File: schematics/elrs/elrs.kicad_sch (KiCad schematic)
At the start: 34 parts, among them U13 ESP32-C3FH4, U14 TLV75533PDQNR, U15 SX1281IMLTRT, X2 CJ17-400001010B20

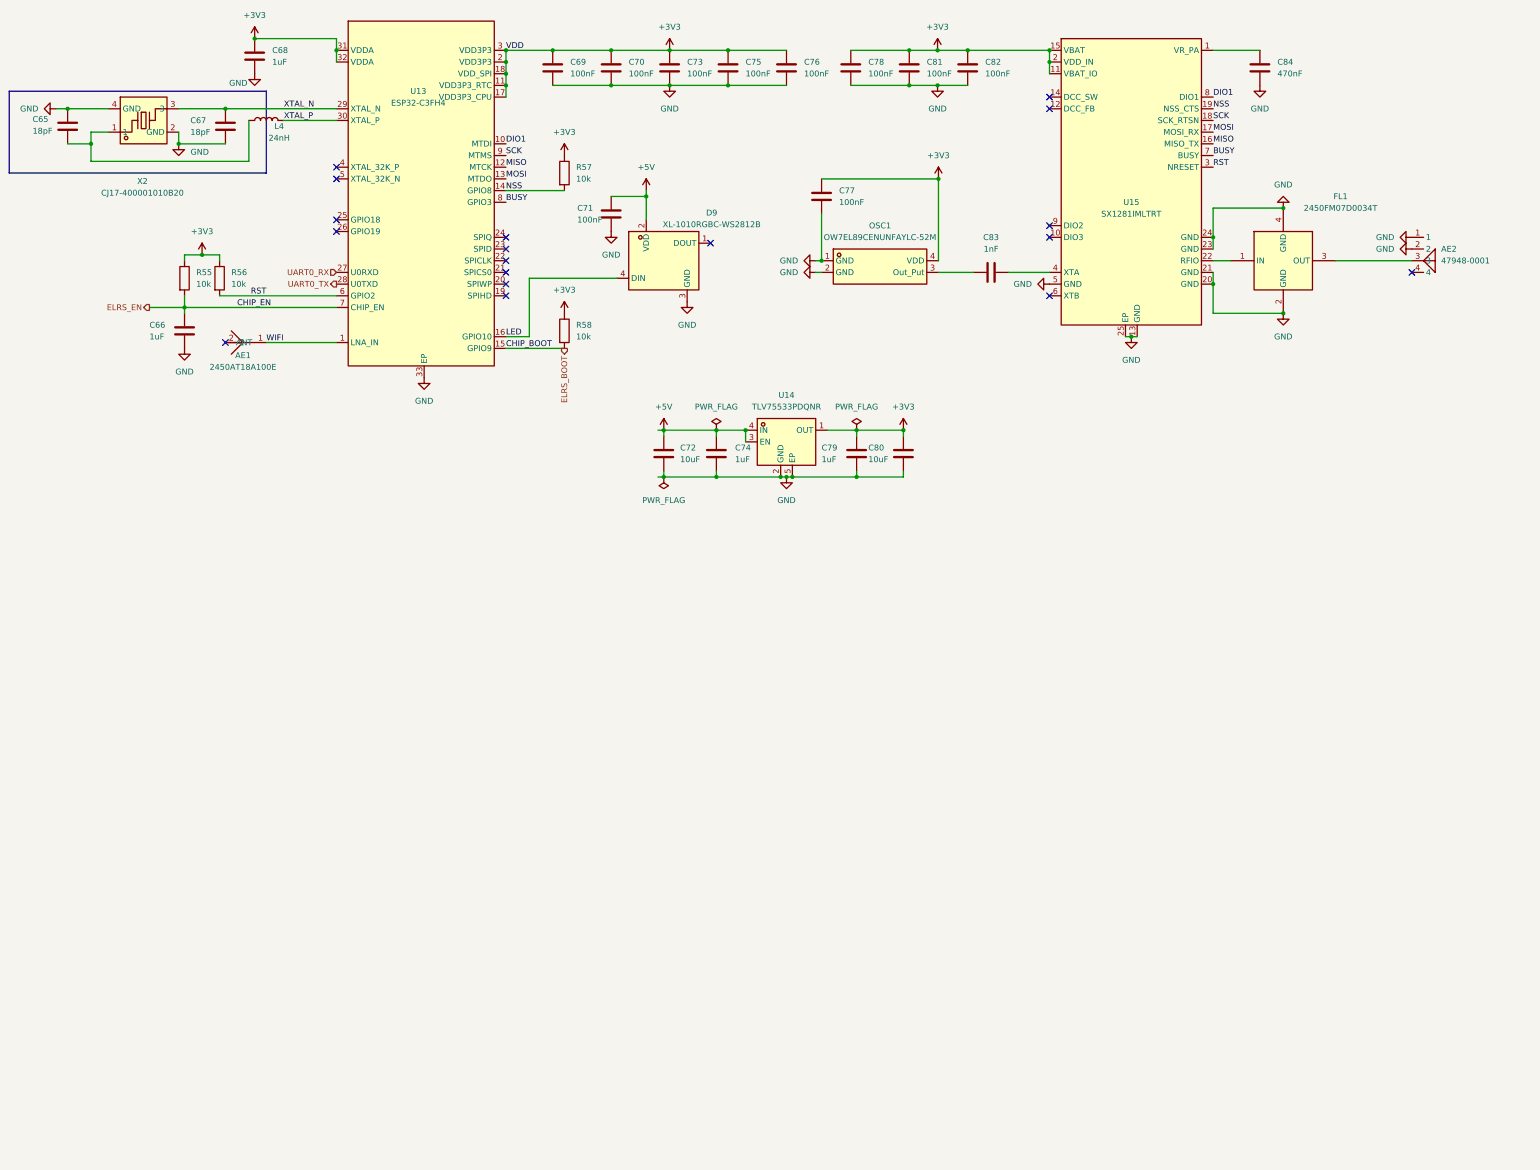
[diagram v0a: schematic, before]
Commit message: checkpoint: Bluejay/BLHeli_S part imports + ESC rework notes
EFM8BB51F16G (C6547511), AGM310MAP (C5184858), BY25Q64ESCIG (C50176394)
imported into libs/lib.kicad_sym + lib.pretty + lib.3dshapes.
BLHELI_S_ESC_NOTES.md documents gate-drive research (1S direct drive vs
2S level-shift requirement) and open design decisions.

Co-Authored-By: Claude Fable 5 <noreply@anthropic.com>
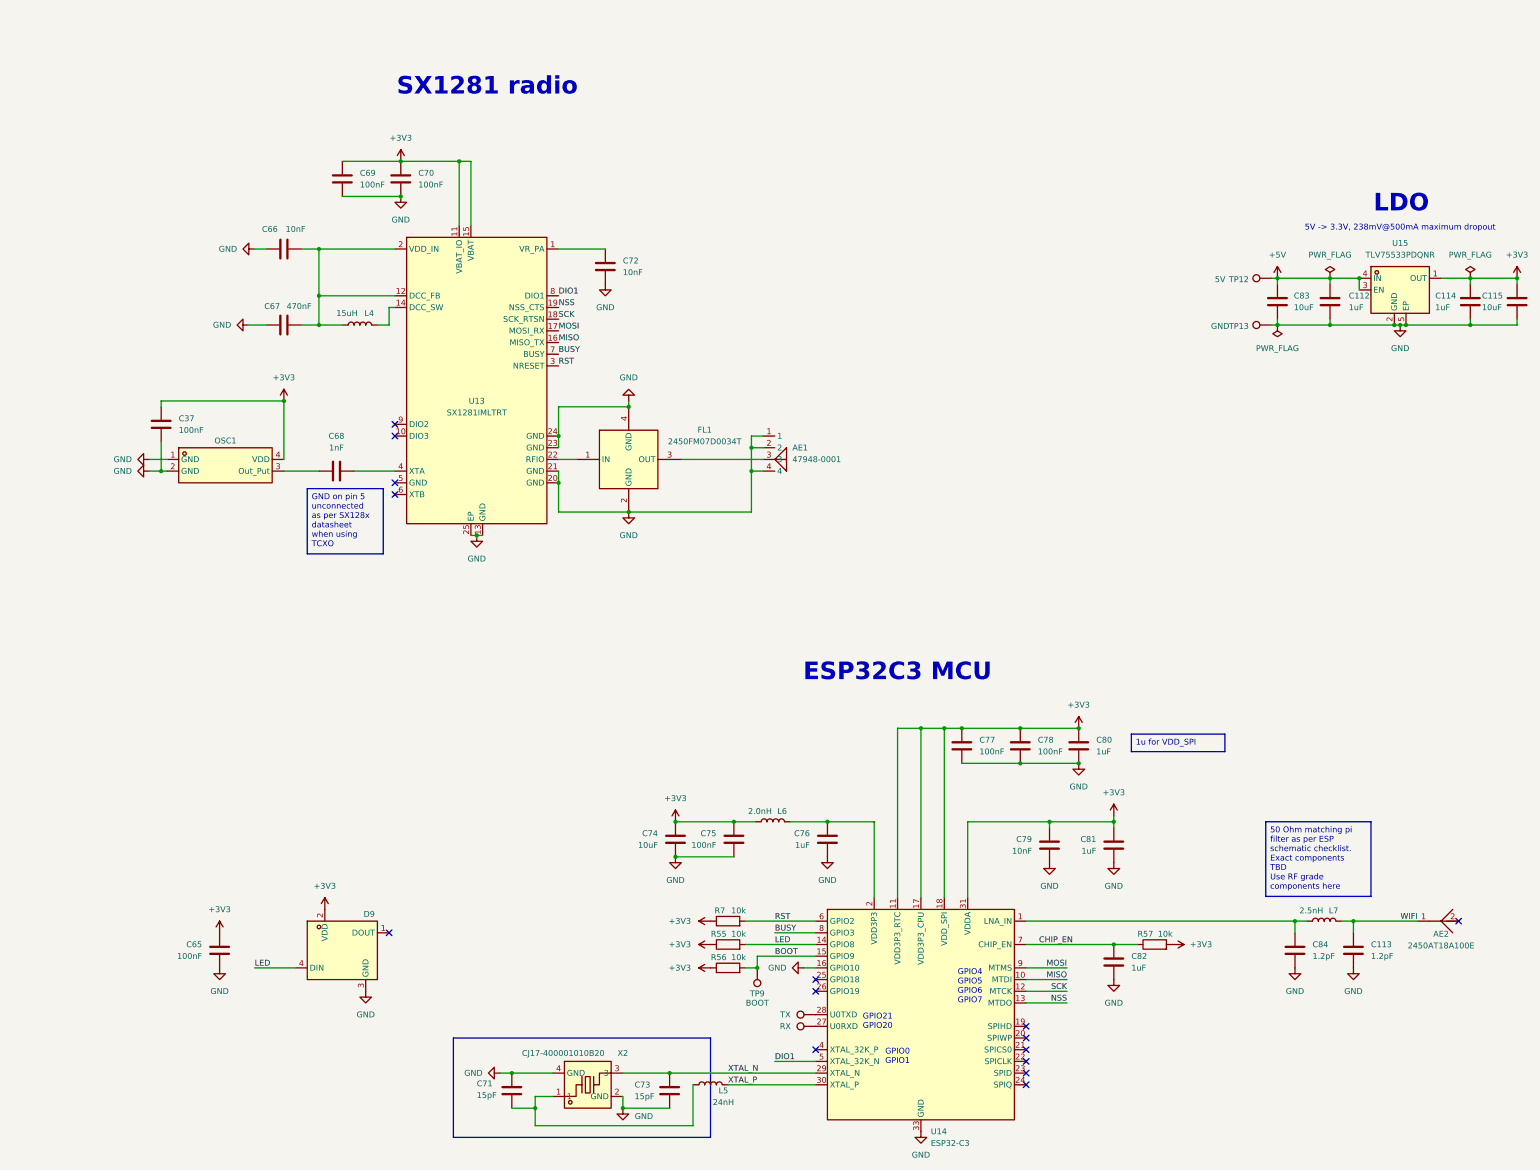
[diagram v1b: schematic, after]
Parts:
- removed AE1: 2450AT18A100E, lib:ANT-SMD_L3.2-W1.6, symbol lib:2450AT18A100E
- removed AE2: 47948-0001, lib:ANT-SMD_47948-0001, symbol lib:47948-0001
- removed C68: 1uF, Capacitor_SMD:C_0201_0603Metric, symbol Device:C
- removed D9: XL-1010RGBC-WS2812B, lib:LED-SMD_4P-L1.0-W1.0-TL_XL-1010RGBC-WS2812B, symbol lib:XL-1010RGBC-WS2812B
- removed FL1: 2450FM07D0034T, lib:FILTER-SMD_4P-L1.0-W0.5-L, symbol lib:2450FM07D0034T
- removed R58: 10k, Resistor_SMD:R_0201_0603Metric, symbol Device:R
- removed U13: ESP32-C3FH4, lib:QFN-32_L5.0-W5.0-P0.50-TL-EP3.7, symbol lib:ESP32-C3FH4
- removed X2: CJ17-400001010B20, lib:CRYSTAL-SMD_4P-L1.6-W1.2-BL, symbol lib:CJ17-400001010B20
- added AE1: 47948-0001, OpenRX-Shared:ANT-SMD_47948-0001, symbol OpenRX-Shared:47948-0001
- added AE2: 2450AT18A100E, OpenRX-Shared:ANT-SMD_L3.2-W1.6, symbol OpenRX-Shared:2450AT18A100E
- added C113: 1.2pF, Capacitor_SMD:C_0201_0603Metric, symbol Device:C
- added C72, C79: 10nF, Capacitor_SMD:C_0201_0603Metric, symbol Device:C
- added C74: 10uF, Capacitor_SMD:C_0402_1005Metric, symbol Device:C
- added C77: 100nF, Capacitor_SMD:C_0201_0603Metric, symbol Device:C
- added C80: 1uF, Capacitor_SMD:C_0201_0603Metric, symbol Device:C
- added D9: XL-1010RGBC-WS2812B, OpenRX-Shared:LED-SMD_4P-L1.0-W1.0-TL_XL-1010RGBC-WS2812B, symbol OpenRX-Shared:XL-1010RGBC-WS2812B
- added FL1: 2450FM07D0034T, OpenRX-Shared:FILTER-SMD_4P-L1.0-W0.5-L, symbol OpenRX-Shared:2450FM07D0034T
- added L5: 24nH, Inductor_SMD:L_0201_0603Metric, symbol Device:L
- added L6: 2.0nH, Inductor_SMD:L_0201_0603Metric, symbol Device:L
- added L7: 2.5nH, Inductor_SMD:L_0201_0603Metric, symbol Device:L
- added R7: 10k, Resistor_SMD:R_0201_0603Metric, symbol Device:R
- added TP10: TX, OpenRX-Shared:SolderPad_1.2x2.0mm, symbol Connector:TestPoint
- added TP11: RX, OpenRX-Shared:SolderPad_1.2x2.0mm, symbol Connector:TestPoint
- added TP12: 5V, OpenRX-Shared:SolderPad_1.2x2.0mm, symbol Connector:TestPoint
- added TP13: GND, OpenRX-Shared:SolderPad_1.2x2.0mm, symbol Connector:TestPoint
- added TP9: BOOT, OpenRX-Shared:SolderPad_1.2x2.0mm, symbol Connector:TestPoint
- added U14: ESP32-C3, Package_DFN_QFN:QFN-32-1EP_5x5mm_P0.5mm_EP3.7x3.7mm, symbol MCU_Espressif:ESP32-C3
- added X2: CJ17-400001010B20, OpenRX-Shared:CRYSTAL-SMD_4P-L1.6-W1.2-BL, symbol OpenRX-Shared:CJ17-400001010B20
- C112: renamed from C74; LCSC Part (none) -> C76935
- C114: renamed from C79; LCSC Part (none) -> C76935
- C115: renamed from C80; LCSC Part (none) -> C15525
- C37: renamed from C77; LCSC Part (none) -> C76939
- C65: value 18pF -> 100nF; LCSC C62164 -> C76939; LCSC Part (none) -> C76939
- C66: value 1uF -> 10nF; LCSC C76935 -> C2168164; LCSC Part (none) -> C2168164
- C67: value 18pF -> 470nF; LCSC C62164 -> C85926; LCSC Part (none) -> C85926
- C68: renamed from C83; LCSC Part (none) -> C66942
- C69, C70, C75, C78: LCSC Part (none) -> C76939
- C71, C73: value 100nF -> 15pF; LCSC C76939 -> C85891; LCSC Part (none) -> C85891
- C76, C81, C82: value 100nF -> 1uF; LCSC C76939 -> C76935; LCSC Part (none) -> C76935
- C83: renamed from C72; LCSC Part (none) -> C15525
- C84: value 470nF -> 1.2pF; LCSC C85926 -> C85895
- L4: value 24nH -> 15uH; footprint Inductor_SMD:L_0201_0603Metric -> Inductor_SMD:L_0805_2012Metric; LCSC C206441 -> (none)
- OSC1: footprint lib:OSC-SMD_4P-L2.0-W1.6-BL_TXC_7Z -> OpenRX-Shared:OSC-SMD_4P-L2.0-W1.6-BL_TXC_7Z; symbol lib:OW7EL89CENUNFAYLC-52M -> OpenRX-Shared:OW7EL89CENUNFAYLC-52M
- R55, R56, R57: LCSC Part (none) -> C106225
- U13: renamed from U15; footprint lib:QFN-24_L4.0-W4.0-P0.50-TL-EP2.6 -> OpenRX-Shared:QFN-24_L4.0-W4.0-P0.50-TL-EP2.6; symbol lib:SX1281IMLTRT -> OpenRX-Shared:SX1281IMLTRT
- U15: renamed from U14; footprint lib:X2SON-4_L1.0-W1.0-P0.65-TL-EP -> OpenRX-Shared:X2SON-4_L1.0-W1.0-P0.65-TL-EP; symbol lib:TLV75533PDQNR -> OpenRX-Shared:TLV75533PDQNR
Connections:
- net +3V3: now also C65.1, R57.2, C74.1, C77.1, C79.1, C80.1, D9.2 (VDD), L6.2, R7.1, U14.11 (VDD3P3_RTC), U14.17 (VDD3P3_CPU), U14.18 (VDD_SPI), U14.31 (VDDA), U14.32 (VDDA); no longer C73.1, C76.1, C82.1, R57.1, U13.2 (VDD_IN)
- net +5V: now also TP12.1; no longer C71.1
- net BUSY: now also U14.8 (GPIO3)
- net DIO1: now also U14.5 (XTAL_32K_N)
- net GND: now also C66.1, C67.1, AE1.1, AE1.2, AE1.4, C113.2, C72.2, C74.2, C77.2, C79.2, C80.2, D9.3 (GND), FL1.2 (GND), FL1.4 (GND), TP13.1, U14.16 (GPIO10), U14.33 (GND), X2.2 (GND), X2.4 (GND); no longer C66.2, C67.2, U13.5 (GND)
- net LED: now also R55.2, D9.4 (DIN), U14.14 (GPIO8)
- net MISO: now also U14.10 (MTDI)
- net MOSI: now also U14.9 (MTMS)
- net NSS: now also U14.13 (MTDO); no longer R57.2
- net RST: now also R7.2, U14.6 (GPIO2); no longer R56.2
- net SCK: now also U14.12 (MTCK)
- net WIFI: now also AE2.1, C113.1, L7.1
- net XTAL_N: now also C73.1, U14.29 (XTAL_N), X2.3; no longer C67.1
- net XTAL_P: now also L5.2, U14.30 (XTAL_P); no longer L4.2
- net at L4.1: now also C66.2, C67.2, U13.12 (DCC_FB), U13.2 (VDD_IN); no longer C65.1
- net at U13.22 (RFIO): now also FL1.1 (IN)
- net at U13.1 (VR_PA): now also C72.1; no longer C84.1
- net at U13.14 (DCC_SW): now also L4.2
- removed net ELRS_EN: C66.1, R55.2
- new net: C71.1, L5.1, X2.1
- new net: C76.1, L6.1, U14.2 (VDD3P3), U14.3 (VDD3P3)
- new net: AE1.3, FL1.3 (OUT)
- new net: C84.1, L7.2, U14.1 (LNA_IN)
- new net: TP11.1, U14.27 (U0RXD)
- new net: TP10.1, U14.28 (U0TXD)
- new net BOOT: R56.2, TP9.1, U14.15 (GPIO9)
- new net CHIP_EN: C82.1, R57.1, U14.7 (CHIP_EN)
- no-connect marks 18 -> 15
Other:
- note added: "5V -> 3.3V, 238mV@500mA maximum dropout"
- note added: "ESP32C3 MCU"
- note added: "GPIO0 GPIO1"
- note added: "GPIO21 GPIO20"
- note added: "GPIO4 GPIO5 GPIO6 GPIO7"
- note added: "LDO"
- note added: "SX1281 radio"
- moved on the sheet: C112, C114, C115, C37, C68, C83, OSC1, U13, U15
